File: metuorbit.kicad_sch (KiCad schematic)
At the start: 20 parts, among them IC1 BLACKPILLF4, IC2 LoRa E220-900T30D, IC3 BNO055, IC4 NEO-M8N, IC5 BMP388, IC6 MicroSD_Reader, IC7 HT7333, IC8 MP1584, J2 BATT Input, J3 SERVO1, J4 SERVO2, Q1 2N3904

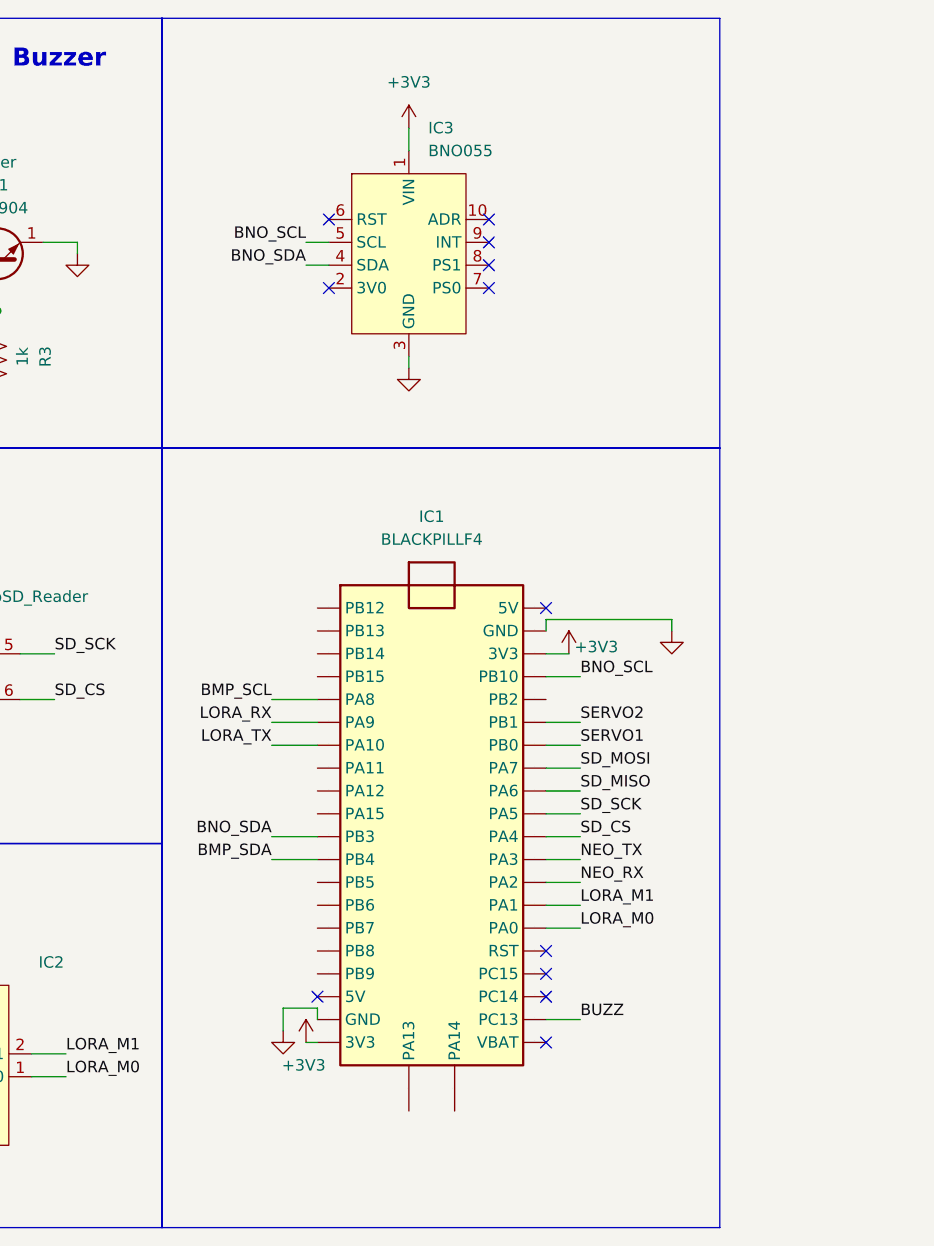
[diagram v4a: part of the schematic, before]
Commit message: Resistive wire trigger is added.
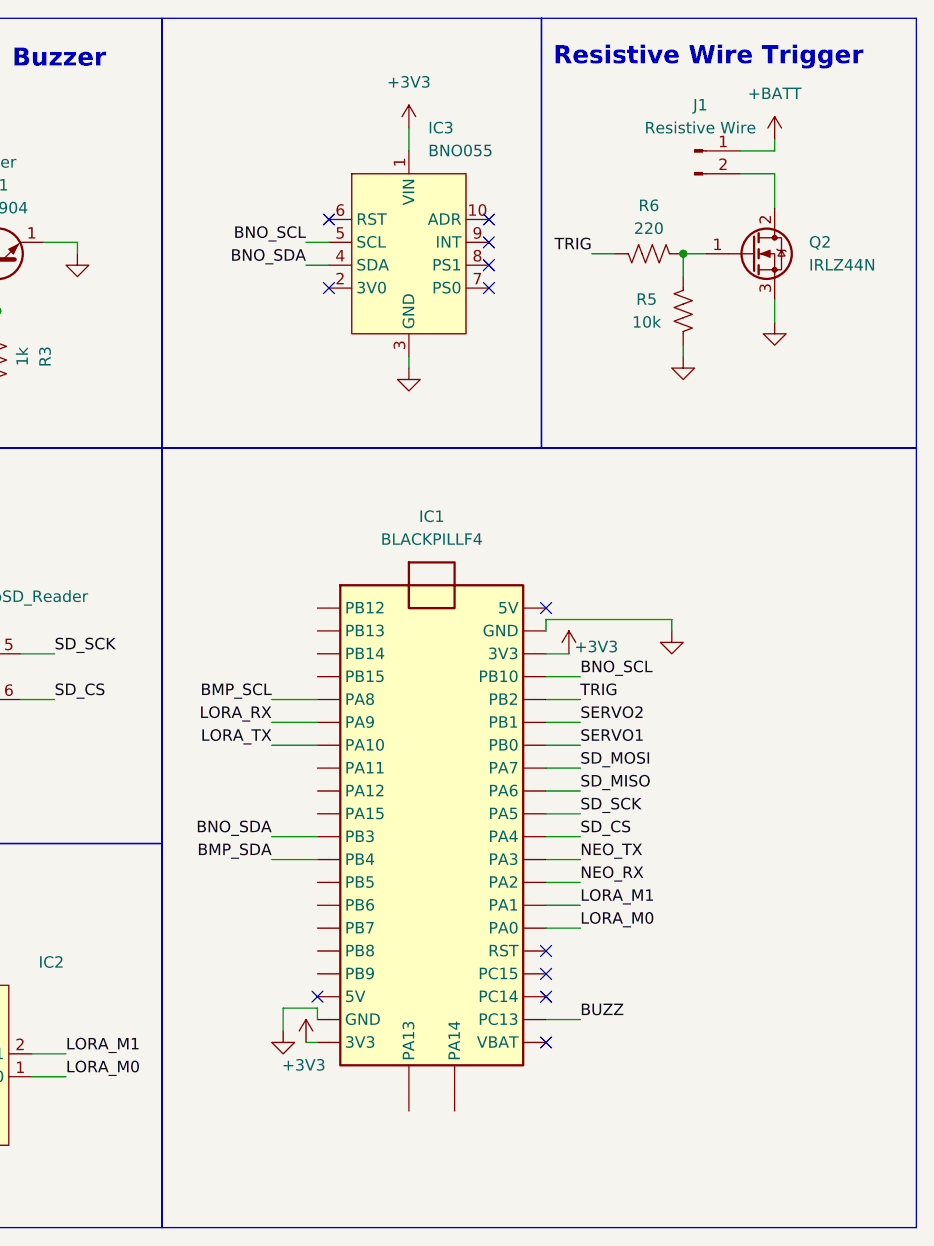
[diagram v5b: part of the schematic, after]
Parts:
- added J1: Resistive Wire, TerminalBlock_Phoenix:TerminalBlock_Phoenix_MKDS-1,5-2-5.08_1x02_P5.08mm_Horizontal, symbol Connector:Conn_01x02_Pin
- added Q2: IRLZ44N, Package_TO_SOT_THT:TO-220-3_Vertical, symbol Transistor_FET:IRLZ44N
- added R5: 10k, Resistor_SMD:R_1206_3216Metric_Pad1.30x1.75mm_HandSolder, symbol Device:R_US
- added R6: 220, Resistor_SMD:R_1206_3216Metric_Pad1.30x1.75mm_HandSolder, symbol Device:R_US
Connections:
- net +BATT: now also J1.1 (Pin_1)
- net GND: now also Q2.3 (S), R5.2
- net TRIG: now reaches IC1.PB2
- net TRIG: now also R6.2
- new net: Q2.1 (G), R5.1, R6.1
- new net: J1.2 (Pin_2), Q2.2 (D)
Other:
- note added: "Resistive Wire Trigger"

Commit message: First design of PCB is done.
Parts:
- added C3: 470u, Capacitor_THT:CP_Radial_D5.0mm_P2.50mm, symbol Device:C_Polarized
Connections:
- net +3V3: now also IC4.1 (VCC); no longer IC4.4 (VCC)
- net +BATT: now also C3.1
- net GND: now also IC4.4 (GND), C3.2; no longer IC4.1 (GND)
- net LORA_RX: now also IC1.PA10; no longer IC1.PA9
- net LORA_TX: now also IC1.PA9; no longer IC1.PA10
- net NEO_RX: now also IC4.2 (RX); no longer IC4.3 (RX)
- net NEO_TX: now also IC4.3 (TX); no longer IC4.2 (TX)
- net TRIG: now also IC1.PB5; no longer IC1.PB2
- no-connect marks 15 -> 16
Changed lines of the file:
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@@
 	)
 	(rectangle
-		(start 112.776 73.66)
+		(start 113.03 73.66)
 		(end 166.878 117.602)
 		(stroke
@@
 	)
 	(rectangle
-		(start 60.198 90.424)
+		(start 60.198 93.472)
 		(end 91.186 117.602)
 		(stroke
@@
 	)
 	(junction
+		(at 77.47 81.28)
+		(diameter 0)
+		(color 0 0 0 0)
+	)
+	(junction
 		(at 74.93 86.36)
 		(diameter 0)
@@
 		(color 0 0 0 0)
 	)
+	(junction
+		(at 77.47 88.9)
+		(diameter 0)
+		(color 0 0 0 0)
+	)
 	(no_connect
 		(at 209.55 132.08)
@@
 	)
 	(no_connect
+		(at 209.55 101.6)
+	)
+	(no_connect
 		(at 203.2 48.26)
 	)
@@
 	(wire
 		(pts
+			(xy 77.47 81.28) (xy 77.47 83.82)
+		)
+		(stroke
+			(width 0)
+			(type default)
+		)
+	)
+	(wire
+		(pts
 			(xy 69.85 110.49) (xy 69.85 113.03)
 		)
@@
 	(wire
 		(pts
+			(xy 77.47 80.01) (xy 77.47 81.28)
+		)
+		(stroke
+			(width 0)
+			(type default)
+		)
+	)
+	(wire
+		(pts
 			(xy 209.55 92.71) (xy 223.52 92.71)
 		)
@@
 	(wire
 		(pts
+			(xy 77.47 88.9) (xy 83.82 88.9)
+		)
+		(stroke
+			(width 0)
+			(type default)
+		)
+	)
+	(wire
+		(pts
 			(xy 100.33 87.63) (xy 102.87 87.63)
 		)
@@
 	(wire
 		(pts
+			(xy 74.93 86.36) (xy 77.47 86.36)
+		)
+		(stroke
+			(width 0)
+			(type default)
+		)
+	)
+	(wire
+		(pts
 			(xy 100.33 100.33) (xy 102.87 100.33)
 		)
@@
 	(wire
 		(pts
-			(xy 209.55 101.6) (xy 213.36 101.6)
+			(xy 179.07 121.92) (xy 184.15 121.92)
 		)
 		(stroke
@@
 	(wire
 		(pts
+			(xy 77.47 81.28) (xy 83.82 81.28)
+		)
+		(stroke
+			(width 0)
+			(type default)
+		)
+	)
+	(wire
+		(pts
 			(xy 72.39 60.96) (xy 72.39 62.23)
 		)
@@
 	(wire
 		(pts
-			(xy 87.63 149.86) (xy 87.63 151.13)
+			(xy 77.47 86.36) (xy 77.47 88.9)
 		)
 		(stroke
@@
 	(wire
 		(pts
-			(xy 74.93 86.36) (xy 77.47 86.36)
+			(xy 87.63 149.86) (xy 87.63 151.13)
 		)
 		(stroke
@@
 	)
 	(label "TRIG"
-		(at 213.36 101.6 0)
+		(at 179.07 121.92 180)
 		(effects
 			(font
 				(size 1.27 1.27)
 			)
-			(justify left bottom)
+			(justify right bottom)
 		)
 	)
@@
 	)
 	(label "LORA_RX"
-		(at 179.07 104.14 180)
+		(at 179.07 106.68 180)
 		(effects
 			(font
@@
 	)
 	(label "LORA_TX"
-		(at 179.07 106.68 180)
+		(at 179.07 104.14 180)
 		(effects
 			(font
@@
 	)
 	(symbol
+		(lib_id "Device:C_Polarized")
+		(at 83.82 85.09 0)
+		(mirror y)
+		(unit 1)
+		(body_style 1)
+		(exclude_from_sim no)
+		(in_bom yes)
+		(on_board yes)
+		(in_pos_files yes)
+		(dnp no)
+		(property "Reference" "C3"
+			(at 87.63 82.9309 0)
+			(show_name no)
+			(do_not_autoplace no)
+			(effects
+				(font
+					(size 1.27 1.27)
+				)
+				(justify right)
+			)
+		)
+		(property "Value" "470u"
+			(at 87.63 85.4709 0)
+			(show_name no)
+			(do_not_autoplace no)
+			(effects
+				(font
+					(size 1.27 1.27)
+				)
+				(justify right)
+			)
+		)
+		(property "Footprint" "Capacitor_THT:CP_Radial_D5.0mm_P2.50mm"
+			(at 82.8548 88.9 0)
+			(hide yes)
+			(show_name no)
+			(do_not_autoplace no)
+			(effects
+				(font
+					(size 1.27 1.27)
+				)
+			)
+		)
+		(property "Datasheet" ""
+			(at 83.82 85.09 0)
+			(hide yes)
+			(show_name no)
+			(do_not_autoplace no)
+			(effects
+				(font
+					(size 1.27 1.27)
+				)
+			)
+		)
+		(property "Description" "Polarized capacitor"
+			(at 83.82 85.09 0)
+			(hide yes)
+			(show_name no)
+			(do_not_autoplace no)
+			(effects
+				(font
+					(size 1.27 1.27)
+				)
+			)
+		)
+		(pin "2"
+		)
+		(pin "1"
+		)
+		(instances
+			(project "metuorbit"
+				(path "/89873f72-2816-48af-bb90-599d5d614f6e"
+					(reference "C3")
+					(unit 1)
+				)
+			)
+		)
+	)
+	(symbol
 		(lib_id "power:PWR_FLAG")
 		(at 96.52 38.1 0)
@@
 	(symbol
 		(lib_id "power:GND")
-		(at 77.47 86.36 0)
+		(at 77.47 88.9 0)
 		(unit 1)
 		(body_style 1)
@@
 		(fields_autoplaced yes)
 		(property "Reference" "#PWR023"
-			(at 77.47 92.71 0)
+			(at 77.47 95.25 0)
 			(hide yes)
 			(show_name no)
@@
 		)
 		(property "Value" "GND"
-			(at 77.47 91.44 0)
+			(at 77.47 93.98 0)
 			(hide yes)
 			(show_name no)
@@
 		)
 		(property "Footprint" ""
-			(at 77.47 86.36 0)
+			(at 77.47 88.9 0)
 			(hide yes)
 			(show_name no)
@@
 		)
 		(property "Datasheet" ""
-			(at 77.47 86.36 0)
+			(at 77.47 88.9 0)
 			(hide yes)
 			(show_name no)
@@
 		)
 		(property "Description" "Power symbol creates a global label with name \"GND\" , ground"
-			(at 77.47 86.36 0)
+			(at 77.47 88.9 0)
 			(hide yes)
 			(show_name no)
@@
 	(symbol
 		(lib_id "power:+BATT")
-		(at 77.47 83.82 0)
+		(at 77.47 80.01 0)
 		(unit 1)
 		(body_style 1)
@@
 		(fields_autoplaced yes)
 		(property "Reference" "#PWR022"
-			(at 77.47 87.63 0)
+			(at 77.47 83.82 0)
 			(hide yes)
 			(show_name no)
@@
 		)
 		(property "Value" "+BATT"
-			(at 77.47 78.74 0)
+			(at 77.47 74.93 0)
 			(show_name no)
 			(do_not_autoplace no)
@@
 		)
 		(property "Footprint" ""
-			(at 77.47 83.82 0)
+			(at 77.47 80.01 0)
 			(hide yes)
 			(show_name no)
@@
 		)
 		(property "Datasheet" ""
-			(at 77.47 83.82 0)
+			(at 77.47 80.01 0)
 			(hide yes)
 			(show_name no)
@@
 		)
 		(property "Description" "Power symbol creates a global label with name \"+BATT\""
-			(at 77.47 83.82 0)
+			(at 77.47 80.01 0)
 			(hide yes)
 			(show_name no)

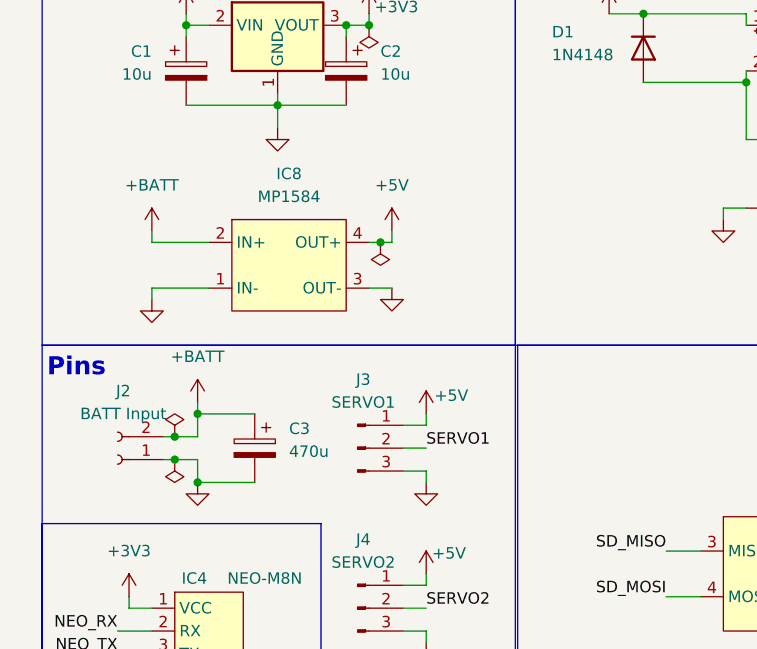
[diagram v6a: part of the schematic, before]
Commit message: PCB is reorganized. Some texts are added.
Checking the design is needed.
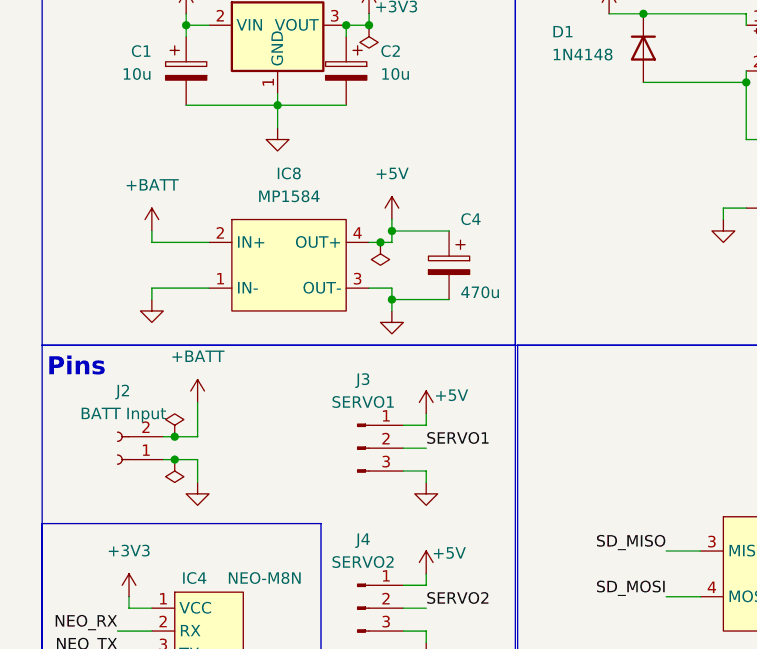
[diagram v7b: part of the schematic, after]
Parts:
- removed C3: 470u, Capacitor_THT:CP_Radial_D5.0mm_P2.50mm, symbol Device:C_Polarized
- added C4: 470u, Capacitor_THT:CP_Radial_D8.0mm_P3.50mm, symbol Device:C_Polarized
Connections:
- net +5V: now also C4.1
- net GND: now also C4.2
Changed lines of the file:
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@@
 	)
 	(junction
-		(at 97.79 62.23)
+		(at 99.06 60.96)
 		(diameter 0)
 		(color 0 0 0 0)
 	)
 	(junction
-		(at 224.79 52.07)
+		(at 99.06 68.58)
 		(diameter 0)
 		(color 0 0 0 0)
 	)
 	(junction
-		(at 93.98 38.1)
+		(at 97.79 62.23)
 		(diameter 0)
 		(color 0 0 0 0)
 	)
 	(junction
-		(at 74.93 83.82)
+		(at 224.79 52.07)
 		(diameter 0)
 		(color 0 0 0 0)
 	)
 	(junction
-		(at 77.47 81.28)
+		(at 93.98 38.1)
 		(diameter 0)
 		(color 0 0 0 0)
 	)
 	(junction
-		(at 74.93 86.36)
+		(at 74.93 83.82)
 		(diameter 0)
 		(color 0 0 0 0)
 	)
 	(junction
-		(at 127 36.83)
+		(at 74.93 86.36)
 		(diameter 0)
 		(color 0 0 0 0)
 	)
 	(junction
-		(at 138.43 44.45)
+		(at 127 36.83)
 		(diameter 0)
 		(color 0 0 0 0)
 	)
 	(junction
-		(at 96.52 38.1)
+		(at 138.43 44.45)
 		(diameter 0)
 		(color 0 0 0 0)
 	)
 	(junction
-		(at 77.47 88.9)
+		(at 96.52 38.1)
 		(diameter 0)
 		(color 0 0 0 0)
@@
 	(wire
 		(pts
-			(xy 77.47 81.28) (xy 77.47 83.82)
+			(xy 77.47 80.01) (xy 77.47 83.82)
 		)
 		(stroke
@@
 	(wire
 		(pts
-			(xy 77.47 80.01) (xy 77.47 81.28)
-		)
-		(stroke
-			(width 0)
-			(type default)
-		)
-	)
-	(wire
-		(pts
 			(xy 209.55 92.71) (xy 223.52 92.71)
 		)
@@
 	(wire
 		(pts
-			(xy 77.47 88.9) (xy 83.82 88.9)
-		)
-		(stroke
-			(width 0)
-			(type default)
-		)
-	)
-	(wire
-		(pts
 			(xy 100.33 87.63) (xy 102.87 87.63)
 		)
@@
 	(wire
 		(pts
+			(xy 99.06 68.58) (xy 99.06 67.31)
+		)
+		(stroke
+			(width 0)
+			(type default)
+		)
+	)
+	(wire
+		(pts
 			(xy 102.87 81.28) (xy 102.87 82.55)
 		)
@@
 	(wire
 		(pts
+			(xy 99.06 69.85) (xy 99.06 68.58)
+		)
+		(stroke
+			(width 0)
+			(type default)
+		)
+	)
+	(wire
+		(pts
 			(xy 179.07 119.38) (xy 184.15 119.38)
 		)
@@
 	(wire
 		(pts
-			(xy 99.06 60.96) (xy 99.06 62.23)
+			(xy 99.06 59.69) (xy 99.06 60.96)
 		)
 		(stroke
@@
 	(wire
 		(pts
+			(xy 99.06 68.58) (xy 105.41 68.58)
+		)
+		(stroke
+			(width 0)
+			(type default)
+		)
+	)
+	(wire
+		(pts
 			(xy 179.07 116.84) (xy 184.15 116.84)
 		)
@@
 	(wire
 		(pts
-			(xy 209.55 106.68) (xy 213.36 106.68)
+			(xy 99.06 60.96) (xy 99.06 62.23)
 		)
 		(stroke
@@
 	(wire
 		(pts
-			(xy 77.47 81.28) (xy 83.82 81.28)
+			(xy 209.55 106.68) (xy 213.36 106.68)
 		)
 		(stroke
@@
 	(wire
 		(pts
+			(xy 99.06 60.96) (xy 105.41 60.96)
+		)
+		(stroke
+			(width 0)
+			(type default)
+		)
+	)
+	(wire
+		(pts
 			(xy 72.39 67.31) (xy 72.39 68.58)
 		)
@@
 	(wire
 		(pts
-			(xy 96.52 67.31) (xy 99.06 67.31)
+			(xy 99.06 67.31) (xy 96.52 67.31)
 		)
 		(stroke
@@
 	)
 	(symbol
-		(lib_id "Device:C_Polarized")
-		(at 83.82 85.09 0)
-		(mirror y)
-		(unit 1)
-		(body_style 1)
-		(exclude_from_sim no)
-		(in_bom yes)
-		(on_board yes)
-		(in_pos_files yes)
-		(dnp no)
-		(property "Reference" "C3"
-			(at 87.63 82.9309 0)
-			(show_name no)
-			(do_not_autoplace no)
-			(effects
-				(font
-					(size 1.27 1.27)
-				)
-				(justify right)
-			)
-		)
-		(property "Value" "470u"
-			(at 87.63 85.4709 0)
-			(show_name no)
-			(do_not_autoplace no)
-			(effects
-				(font
-					(size 1.27 1.27)
-				)
-				(justify right)
-			)
-		)
-		(property "Footprint" "Capacitor_THT:CP_Radial_D5.0mm_P2.50mm"
-			(at 82.8548 88.9 0)
-			(hide yes)
-			(show_name no)
-			(do_not_autoplace no)
-			(effects
-				(font
-					(size 1.27 1.27)
-				)
-			)
-		)
-		(property "Datasheet" ""
-			(at 83.82 85.09 0)
-			(hide yes)
-			(show_name no)
-			(do_not_autoplace no)
-			(effects
-				(font
-					(size 1.27 1.27)
-				)
-			)
-		)
-		(property "Description" "Polarized capacitor"
-			(at 83.82 85.09 0)
-			(hide yes)
-			(show_name no)
-			(do_not_autoplace no)
-			(effects
-				(font
-					(size 1.27 1.27)
-				)
-			)
-		)
-		(pin "2"
-		)
-		(pin "1"
-		)
-		(instances
-			(project "metuorbit"
-				(path "/89873f72-2816-48af-bb90-599d5d614f6e"
-					(reference "C3")
-					(unit 1)
-				)
-			)
-		)
-	)
-	(symbol
 		(lib_id "power:PWR_FLAG")
 		(at 96.52 38.1 0)
@@
 	)
 	(symbol
+		(lib_id "Device:C_Polarized")
+		(at 105.41 64.77 0)
+		(mirror y)
+		(unit 1)
+		(body_style 1)
+		(exclude_from_sim no)
+		(in_bom yes)
+		(on_board yes)
+		(in_pos_files yes)
+		(dnp no)
+		(property "Reference" "C4"
+			(at 106.68 59.69 0)
+			(show_name no)
+			(do_not_autoplace no)
+			(effects
+				(font
+					(size 1.27 1.27)
+				)
+				(justify right)
+			)
+		)
+		(property "Value" "470u"
+			(at 106.68 67.818 0)
+			(show_name no)
+			(do_not_autoplace no)
+			(effects
+				(font
+					(size 1.27 1.27)
+				)
+				(justify right)
+			)
+		)
+		(property "Footprint" "Capacitor_THT:CP_Radial_D8.0mm_P3.50mm"
+			(at 104.4448 68.58 0)
+			(hide yes)
+			(show_name no)
+			(do_not_autoplace no)
+			(effects
+				(font
+					(size 1.27 1.27)
+				)
+			)
+		)
+		(property "Datasheet" ""
+			(at 105.41 64.77 0)
+			(hide yes)
+			(show_name no)
+			(do_not_autoplace no)
+			(effects
+				(font
+					(size 1.27 1.27)
+				)
+			)
+		)
+		(property "Description" "Polarized capacitor"
+			(at 105.41 64.77 0)
+			(hide yes)
+			(show_name no)
+			(do_not_autoplace no)
+			(effects
+				(font
+					(size 1.27 1.27)
+				)
+			)
+		)
+		(pin "2"
+		)
+		(pin "1"
+		)
+		(instances
+			(project "metuorbit"
+				(path "/89873f72-2816-48af-bb90-599d5d614f6e"
+					(reference "C4")
+					(unit 1)
+				)
+			)
+		)
+	)
+	(symbol
 		(lib_id "power:PWR_FLAG")
 		(at 74.93 83.82 0)
@@
 	(symbol
 		(lib_id "power:GND")
-		(at 99.06 67.31 0)
+		(at 99.06 69.85 0)
 		(unit 1)
 		(body_style 1)
@@
 		(fields_autoplaced yes)
 		(property "Reference" "#PWR020"
-			(at 99.06 73.66 0)
+			(at 99.06 76.2 0)
 			(hide yes)
 			(show_name no)
@@
 		)
 		(property "Value" "GND"
-			(at 99.06 72.39 0)
+			(at 99.06 74.93 0)
 			(hide yes)
 			(show_name no)
@@
 		)
 		(property "Footprint" ""
-			(at 99.06 67.31 0)
+			(at 99.06 69.85 0)
 			(hide yes)
 			(show_name no)
@@
 		)
 		(property "Datasheet" ""
-			(at 99.06 67.31 0)
+			(at 99.06 69.85 0)
 			(hide yes)
 			(show_name no)
@@
 		)
 		(property "Description" "Power symbol creates a global label with name \"GND\" , ground"
-			(at 99.06 67.31 0)
+			(at 99.06 69.85 0)
 			(hide yes)
 			(show_name no)
@@
 	(symbol
 		(lib_id "power:+5V")
-		(at 99.06 60.96 0)
+		(at 99.06 59.69 0)
 		(unit 1)
 		(body_style 1)
@@
 		(fields_autoplaced yes)
 		(property "Reference" "#PWR021"
-			(at 99.06 64.77 0)
+			(at 99.06 63.5 0)
 			(hide yes)
 			(show_name no)
@@
 		)
 		(property "Value" "+5V"
-			(at 99.06 55.88 0)
+			(at 99.06 54.61 0)
 			(show_name no)
 			(do_not_autoplace no)
@@
 		)
 		(property "Footprint" ""
-			(at 99.06 60.96 0)
+			(at 99.06 59.69 0)
 			(hide yes)
 			(show_name no)
@@
 		)
 		(property "Datasheet" ""
-			(at 99.06 60.96 0)
+			(at 99.06 59.69 0)
 			(hide yes)
 			(show_name no)
@@
 		)
 		(property "Description" "Power symbol creates a global label with name \"+5V\""
-			(at 99.06 60.96 0)
+			(at 99.06 59.69 0)
 			(hide yes)
 			(show_name no)

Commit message: LEDs for power lines are added. Some connections are adjusted.
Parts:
- added D2, D3: LED, LED_SMD:LED_1206_3216Metric_Pad1.42x1.75mm_HandSolder, symbol Device:LED
- added R7, R8: 220, Resistor_SMD:R_1206_3216Metric_Pad1.30x1.75mm_HandSolder, symbol Device:R_US
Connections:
- net +3V3: now also D3.2 (A)
- net +5V: now also D2.2 (A)
- net BUZZ: now also IC1.PB9; no longer IC1.PC13
- net GND: now also R7.2, R8.2
- new net: D2.1 (K), R7.1
- new net: D3.1 (K), R8.1
- no-connect marks 16 -> 29
